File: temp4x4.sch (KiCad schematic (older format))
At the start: 17 parts

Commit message: updated schematic
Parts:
- removed J? (x3): 4-wire RTD, symbol Connector:Screw_Terminal_01x04
- added C? (x9): C, symbol Device:C
- added J?: 4-wire RTD, symbol Connector:Screw_Terminal_01x04
- added R? (x7): R, symbol Device:R
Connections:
- net Earth: now also C?.1, C?.1, C?.1, C?.2, C?.2, C?.2
- net ENABLE: now reaches U?.3 (EN)
- net ENABLE: now also J?.6 (Pin_6)
- net at U?.29 (REFN0): now also C?.2, C?.2, R?.2
- net at U?.3 (AIN4): now also C?.2, C?.2, R?.2
- net at U?.30 (REFP0): now also C?.1, C?.1, R?.2
- net at U?.4 (AIN3): now also C?.1, C?.1, R?.2
- net at U?.5 (AIN2): now also C?.2, C?.2, R?.2
- net at U?.6 (AIN1): now also C?.1, C?.1, R?.2
- net at U?.7 (AIN0): now also J?.1 (Pin_1)
- net at J?.2 (Pin_2): now also R?.1
- net at J?.3 (Pin_3): now also R?.1
- net at J?.4 (Pin_4): now also J?.1 (Pin_1)
- new net: J?.2 (Pin_2), R?.1
- new net: J?.3 (Pin_3), R?.1
- new net: J?.4 (Pin_4), R?.1, R?.1
- new net: R?.1, R?.2
- no-connect marks 5 -> 4
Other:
- moved on the sheet: C?, J?

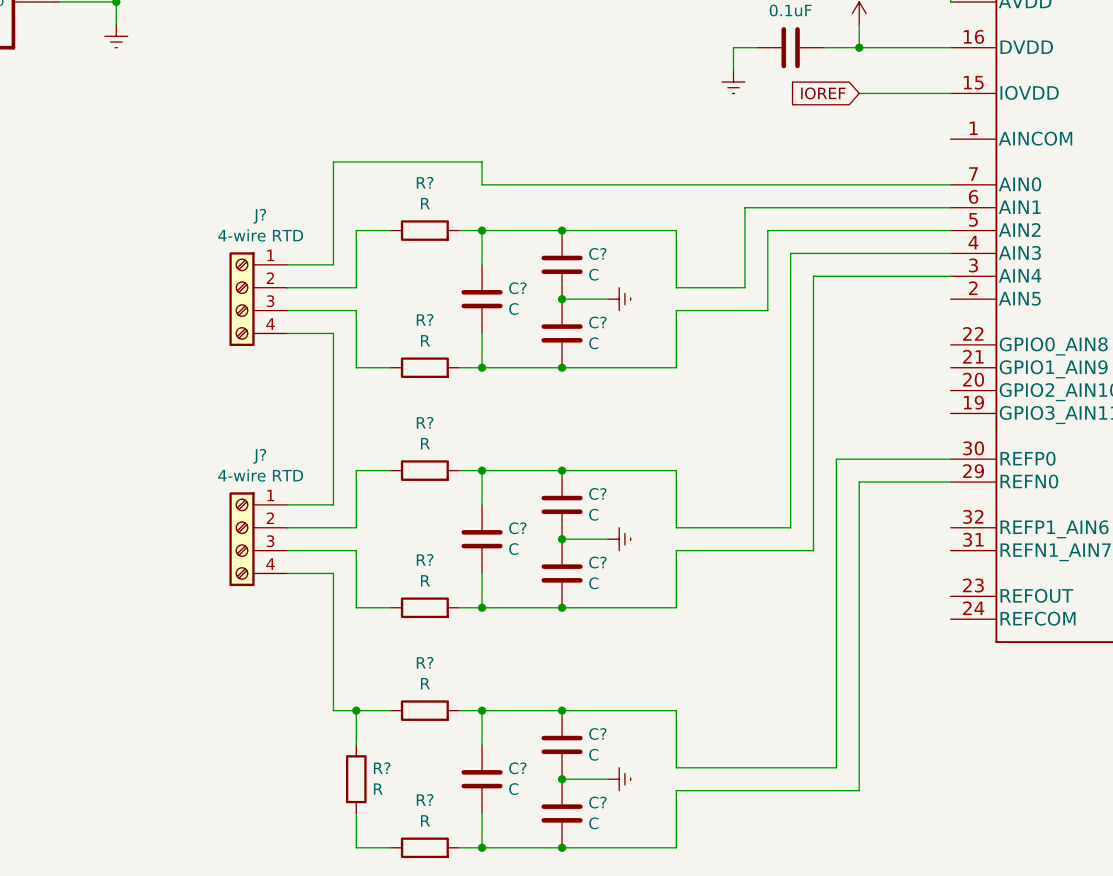
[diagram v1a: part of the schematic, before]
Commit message: added hierarchical sheet for RTDs
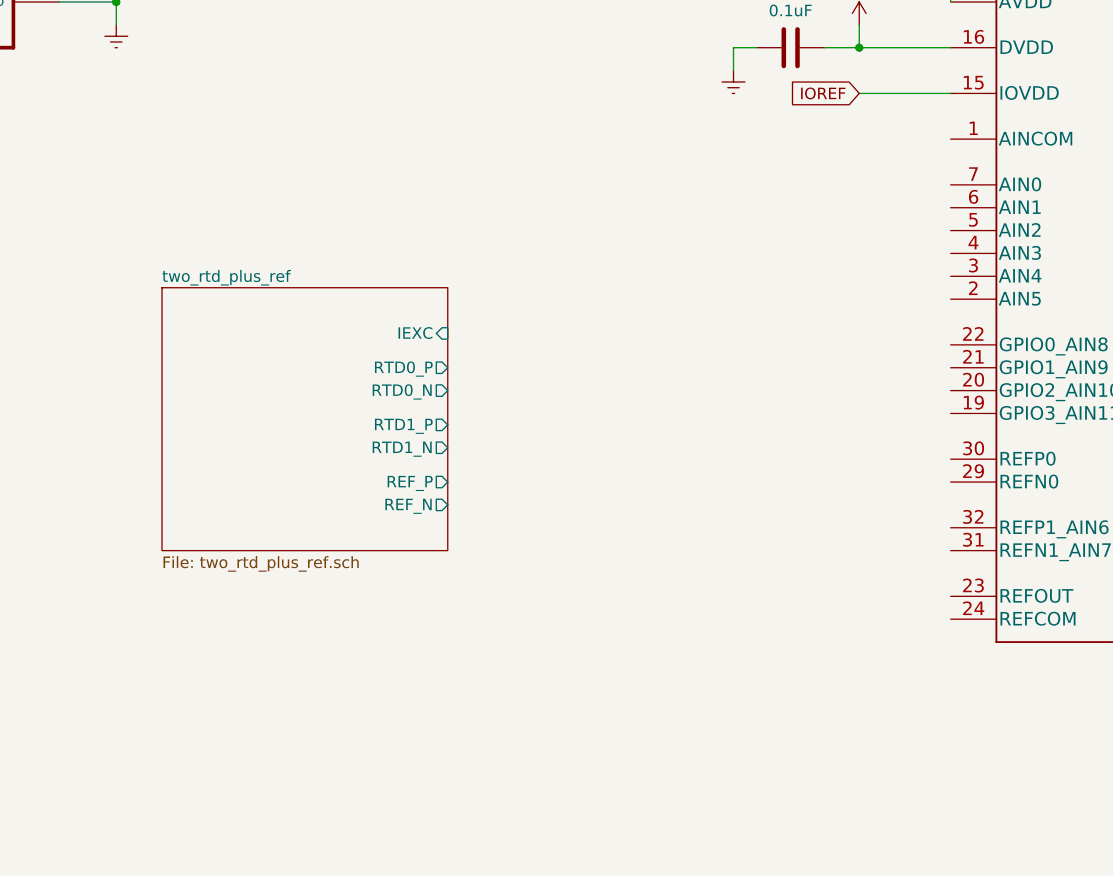
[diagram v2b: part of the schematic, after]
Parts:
- removed C? (x9): C, symbol Device:C
- removed J? (x2): 4-wire RTD, symbol Connector:Screw_Terminal_01x04
- removed R? (x7): R, symbol Device:R

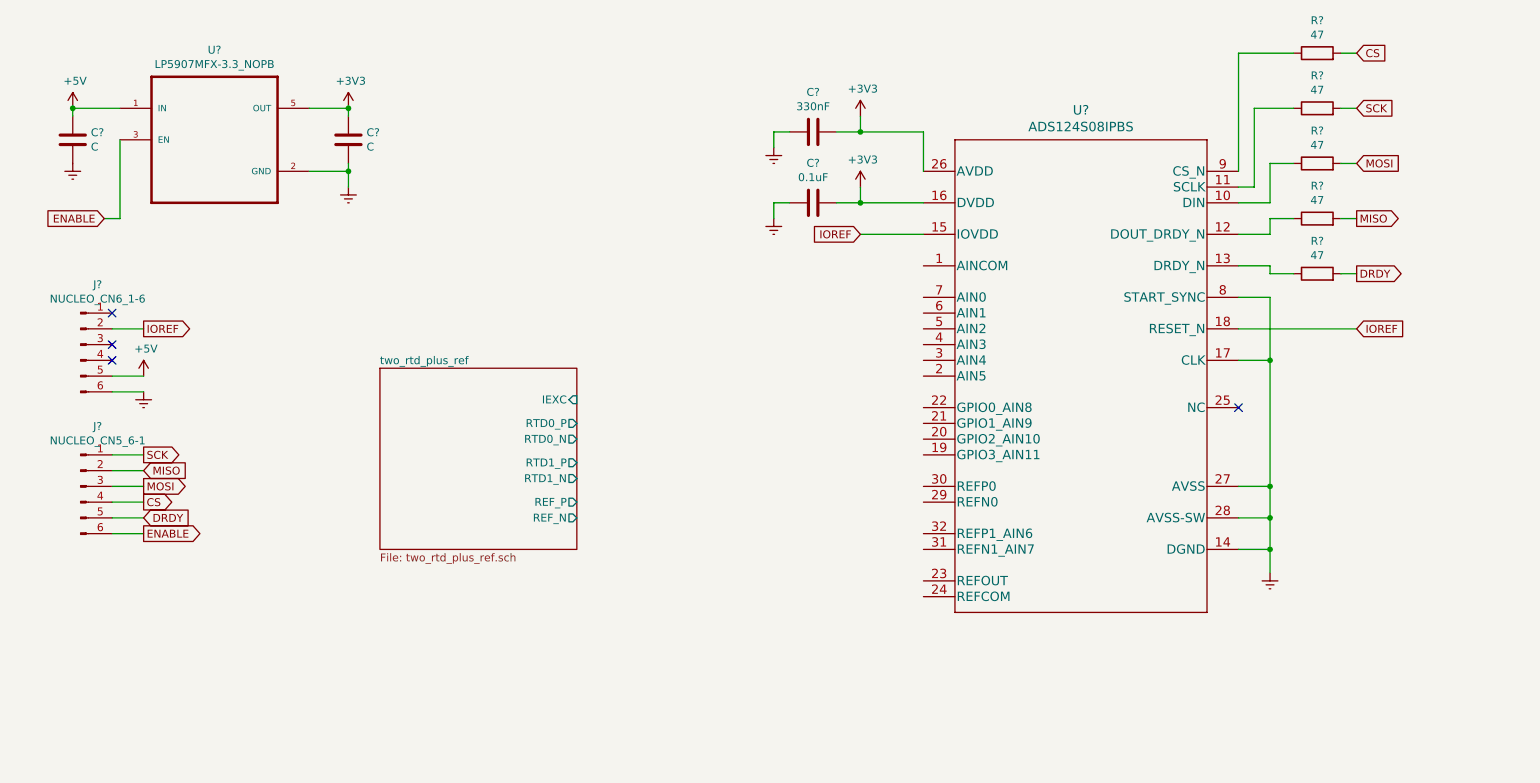
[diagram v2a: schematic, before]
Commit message: Added second set of RTDs
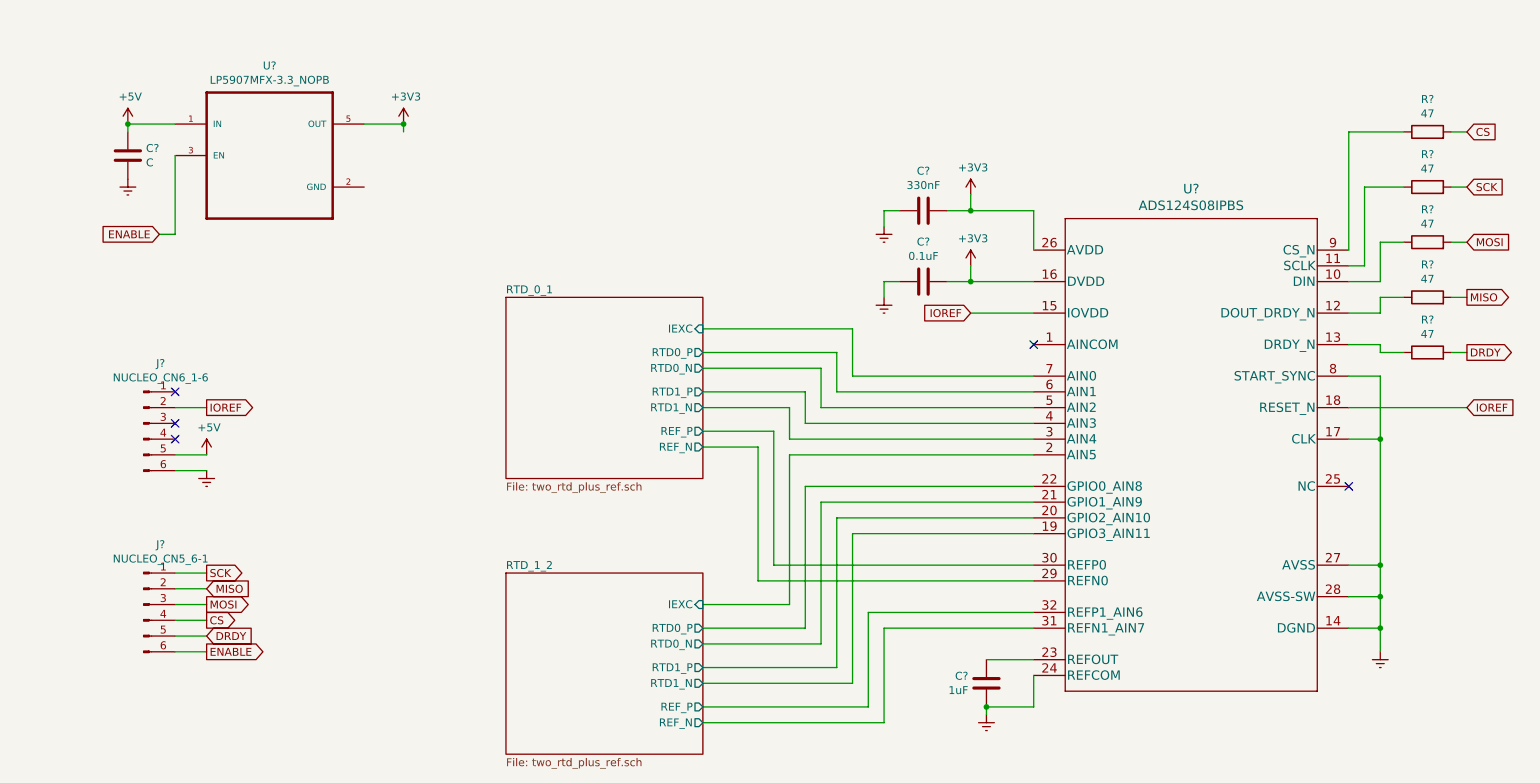
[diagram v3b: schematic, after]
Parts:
- C?: value C -> 1uF
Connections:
- net +3V3: no longer C?.1
- net Earth: now also U?.24 (REFCOM); no longer U?.2 (GND)
- net RTD_1_2/RTD1_N: now reaches U?.19 (GPIO3_AIN11)
- net RTD_1_2/IEXC: now reaches U?.2 (AIN5)
- net RTD_1_2/RTD1_P: now reaches U?.20 (GPIO2_AIN10)
- net RTD_1_2/RTD0_N: now reaches U?.21 (GPIO1_AIN9)
- net RTD_1_2/RTD0_P: now reaches U?.22 (GPIO0_AIN8)
- net at U?.23 (REFOUT): now also C?.1
- net RTD_0_1/REF_N: now reaches U?.29 (REFN0)
- net RTD_0_1/RTD1_N: now reaches U?.3 (AIN4)
- net RTD_0_1/REF_P: now reaches U?.30 (REFP0)
- net RTD_1_2/REF_N: now reaches U?.31 (REFN1_AIN7)
- net RTD_1_2/REF_P: now reaches U?.32 (REFP1_AIN6)
- net RTD_0_1/RTD1_P: now reaches U?.4 (AIN3)
- net RTD_0_1/RTD0_N: now reaches U?.5 (AIN2)
- net RTD_0_1/RTD0_P: now reaches U?.6 (AIN1)
- net RTD_0_1/IEXC: now reaches U?.7 (AIN0)
- no-connect marks 4 -> 5
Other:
- moved on the sheet: C?, J?, R?, U?

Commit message: completed schematic
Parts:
- added C2: 1uF, symbol Device:C
- added C5: 0.1uF, symbol Device:C
- C1: renamed from C?; value C -> 1uF
- gave numbers to parts that had none: 12
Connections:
- net +3V3: now also C2.1
- net Earth: now also U1.2 (GND), C2.2, C5.1
- net IOREF: now also C5.2
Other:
- moved on the sheet: C3, C4

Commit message: finished schematic, assigned footprints, generated netlist
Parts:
- C1, C2, C3, C4, C5, C6: footprint (none) -> Capacitor_SMD:C_0805_2012Metric_Pad1.15x1.40mm_HandSolder
- J1, J2: footprint (none) -> Connector_PinHeader_2.54mm:PinHeader_1x06_P2.54mm_Vertical
- R1, R2, R3, R4, R5: footprint (none) -> Resistor_SMD:R_0805_2012Metric_Pad1.15x1.40mm_HandSolder
- U1: footprint SOT95P280X145-5N -> Package_TO_SOT_SMD:SOT-23-5_HandSoldering
- U2: footprint PBS0032A_N -> Package_QFP:LQFP-32_5x5mm_P0.5mm
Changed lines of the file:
@@
 F 0 "U1" H 2150 2020 50  0000 C CNN
 F 1 "LP5907MFX-3.3_NOPB" H 2150 1929 50  0000 C CNN
-F 2 "SOT95P280X145-5N" H 2150 1450 50  0001 L BNN
+F 2 "Package_TO_SOT_SMD:SOT-23-5_HandSoldering" H 2150 1450 50  0001 L BNN
 F 3 "LP5907MFX-3.3/NOPB" H 2150 1450 50  0001 L BNN
 F 4 "SOT-23 Texas Instruments" H 2150 1450 50  0001 L BNN "Field4"
@@
 F 0 "C1" H 1365 1496 50  0000 L CNN
 F 1 "1uF" H 1365 1405 50  0000 L CNN
-F 2 "" H 1288 1300 50  0001 C CNN
+F 2 "Capacitor_SMD:C_0805_2012Metric_Pad1.15x1.40mm_HandSolder" H 1288 1300 50  0001 C CNN
 F 3 "~" H 1250 1450 50  0001 C CNN
 	1    1250 1450
@@
 F 0 "C6" H 6815 4846 50  0000 L CNN
 F 1 "1uF" H 6815 4755 50  0000 L CNN
-F 2 "" H 6738 4650 50  0001 C CNN
+F 2 "Capacitor_SMD:C_0805_2012Metric_Pad1.15x1.40mm_HandSolder" H 6738 4650 50  0001 C CNN
 F 3 "~" H 6700 4800 50  0001 C CNN
 	1    6700 4800
@@
 F 0 "R1" V 9707 1300 50  0000 C CNN
 F 1 "47" V 9616 1300 50  0000 C CNN
-F 2 "" V 9430 1300 50  0001 C CNN
+F 2 "Resistor_SMD:R_0805_2012Metric_Pad1.15x1.40mm_HandSolder" V 9430 1300 50  0001 C CNN
 F 3 "~" H 9500 1300 50  0001 C CNN
 	1    9500 1300
@@
 F 0 "R2" V 9707 1650 50  0000 C CNN
 F 1 "47" V 9616 1650 50  0000 C CNN
-F 2 "" V 9430 1650 50  0001 C CNN
+F 2 "Resistor_SMD:R_0805_2012Metric_Pad1.15x1.40mm_HandSolder" V 9430 1650 50  0001 C CNN
 F 3 "~" H 9500 1650 50  0001 C CNN
 	1    9500 1650
@@
 F 0 "R3" V 9707 2000 50  0000 C CNN
 F 1 "47" V 9616 2000 50  0000 C CNN
-F 2 "" V 9430 2000 50  0001 C CNN
+F 2 "Resistor_SMD:R_0805_2012Metric_Pad1.15x1.40mm_HandSolder" V 9430 2000 50  0001 C CNN
 F 3 "~" H 9500 2000 50  0001 C CNN
 	1    9500 2000
@@
 F 0 "R4" V 9707 2350 50  0000 C CNN
 F 1 "47" V 9616 2350 50  0000 C CNN
-F 2 "" V 9430 2350 50  0001 C CNN
+F 2 "Resistor_SMD:R_0805_2012Metric_Pad1.15x1.40mm_HandSolder" V 9430 2350 50  0001 C CNN
 F 3 "~" H 9500 2350 50  0001 C CNN
 	1    9500 2350
@@
 F 0 "R5" V 9707 2700 50  0000 C CNN
 F 1 "47" V 9616 2700 50  0000 C CNN
-F 2 "" V 9430 2700 50  0001 C CNN
+F 2 "Resistor_SMD:R_0805_2012Metric_Pad1.15x1.40mm_HandSolder" V 9430 2700 50  0001 C CNN
 F 3 "~" H 9500 2700 50  0001 C CNN
 	1    9500 2700
@@
 F 0 "J1" H 1322 3124 50  0000 R CNN
 F 1 "NUCLEO_CN6_1-6" H 1322 3033 50  0000 R CNN
-F 2 "" H 1350 3150 50  0001 C CNN
+F 2 "Connector_PinHeader_2.54mm:PinHeader_1x06_P2.54mm_Vertical" H 1350 3150 50  0001 C CNN
 F 3 "~" H 1350 3150 50  0001 C CNN
 	1    1350 3150
@@
 F 0 "J2" H 1322 4274 50  0000 R CNN
 F 1 "NUCLEO_CN5_6-1" H 1322 4183 50  0000 R CNN
-F 2 "" H 1350 4300 50  0001 C CNN
+F 2 "Connector_PinHeader_2.54mm:PinHeader_1x06_P2.54mm_Vertical" H 1350 4300 50  0001 C CNN
 F 3 "~" H 1350 4300 50  0001 C CNN
 	1    1350 4300
@@
 F 0 "C4" V 6102 1550 50  0000 C CNN
 F 1 "0.1uF" V 6011 1550 50  0000 C CNN
-F 2 "" H 5888 1400 50  0001 C CNN
+F 2 "Capacitor_SMD:C_0805_2012Metric_Pad1.15x1.40mm_HandSolder" H 5888 1400 50  0001 C CNN
 F 3 "~" H 5850 1550 50  0001 C CNN
 	1    5850 1550
@@
 F 0 "C3" V 6102 1100 50  0000 C CNN
 F 1 "330nF" V 6011 1100 50  0000 C CNN
-F 2 "" H 5888 950 50  0001 C CNN
+F 2 "Capacitor_SMD:C_0805_2012Metric_Pad1.15x1.40mm_HandSolder" H 5888 950 50  0001 C CNN
 F 3 "~" H 5850 1100 50  0001 C CNN
 	1    5850 1100
@@
 F 0 "U2" H 8000 5038 60  0000 C CNN
 F 1 "ADS124S08IPBS" H 8000 4932 60  0000 C CNN
-F 2 "PBS0032A_N" H 8000 3290 60  0001 C CNN
+F 2 "Package_QFP:LQFP-32_5x5mm_P0.5mm" H 8000 3290 60  0001 C CNN
 F 3 "" H 8000 3350 60  0000 C CNN
 	1    8000 3350
@@
 F 0 "C2" H 3115 1496 50  0000 L CNN
 F 1 "1uF" H 3115 1405 50  0000 L CNN
-F 2 "" H 3038 1300 50  0001 C CNN
+F 2 "Capacitor_SMD:C_0805_2012Metric_Pad1.15x1.40mm_HandSolder" H 3038 1300 50  0001 C CNN
 F 3 "~" H 3000 1450 50  0001 C CNN
 	1    3000 1450
@@
 F 0 "C5" V 6102 2000 50  0000 C CNN
 F 1 "0.1uF" V 6011 2000 50  0000 C CNN
-F 2 "" H 5888 1850 50  0001 C CNN
+F 2 "Capacitor_SMD:C_0805_2012Metric_Pad1.15x1.40mm_HandSolder" H 5888 1850 50  0001 C CNN
 F 3 "~" H 5850 2000 50  0001 C CNN
 	1    5850 2000

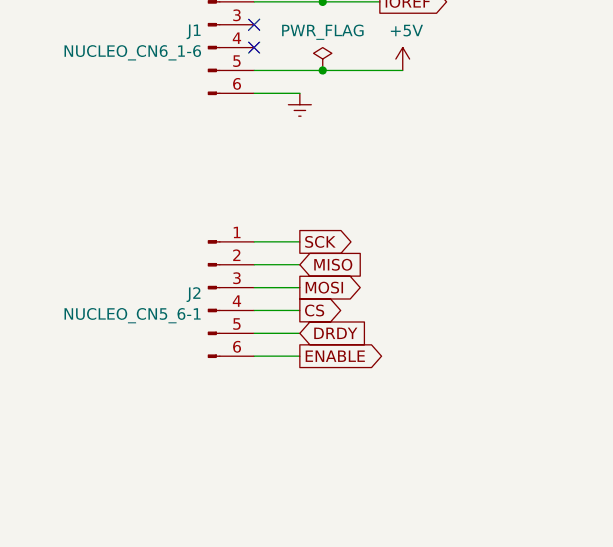
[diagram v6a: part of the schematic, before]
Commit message: made board bigger to allow for better separation of analog / digital domains
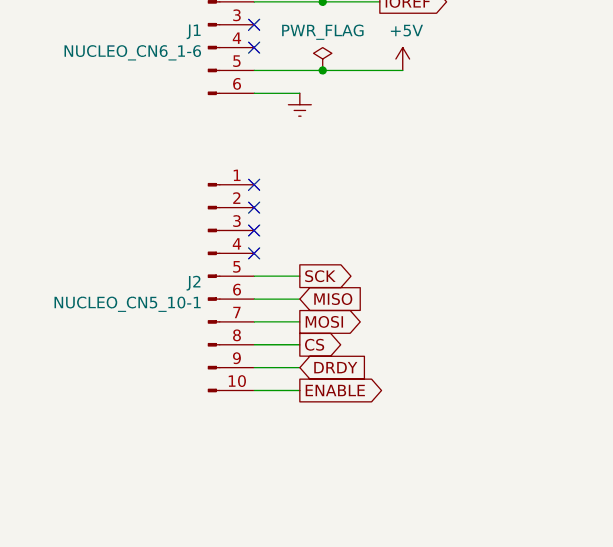
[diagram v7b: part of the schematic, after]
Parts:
- removed J2: NUCLEO_CN5_6-1, Connector_PinHeader_2.54mm:PinHeader_1x06_P2.54mm_Vertical, symbol Connector:Conn_01x06_Male
- added J2: NUCLEO_CN5_10-1, Connector_PinHeader_2.54mm:PinHeader_1x10_P2.54mm_Vertical, symbol Connector:Conn_01x10_Male
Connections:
- net CS: now also J2.8 (Pin_8)
- net DRDY: now also J2.9 (Pin_9)
- net ENABLE: now also J2.10 (Pin_10)
- net MISO: now also J2.6 (Pin_6)
- net MOSI: now also J2.7 (Pin_7)
- net SCK: now also J2.5 (Pin_5)
- no-connect marks 5 -> 9
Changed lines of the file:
@@
 Text GLabel 2100 3050 2    50   Output ~ 0
 IOREF
-Text GLabel 1750 4100 2    50   Output ~ 0
+Text GLabel 1750 4250 2    50   Output ~ 0
 SCK
 $Comp
@@
 	1550 3450 1750 3450
 Wire Wire Line
-	1550 4100 1750 4100
-Wire Wire Line
-	1550 4500 1750 4500
-Wire Wire Line
-	1550 4400 1750 4400
-Wire Wire Line
-	1550 4300 1750 4300
-Wire Wire Line
-	1550 4200 1750 4200
-Text GLabel 1750 4500 2    50   Input ~ 0
+	1550 4250 1750 4250
+Wire Wire Line
+	1550 4650 1750 4650
+Wire Wire Line
+	1550 4550 1750 4550
+Wire Wire Line
+	1550 4450 1750 4450
+Wire Wire Line
+	1550 4350 1750 4350
+Text GLabel 1750 4650 2    50   Input ~ 0
 DRDY
-Text GLabel 1750 4400 2    50   Output ~ 0
+Text GLabel 1750 4550 2    50   Output ~ 0
 CS
-Text GLabel 1750 4300 2    50   Output ~ 0
+Text GLabel 1750 4450 2    50   Output ~ 0
 MOSI
-Text GLabel 1750 4200 2    50   Input ~ 0
+Text GLabel 1750 4350 2    50   Input ~ 0
 MISO
-$Comp
-L Connector:Conn_01x06_Male J2
-U 1 1 5ECC8F38
-P 1350 4300
-F 0 "J2" H 1322 4274 50  0000 R CNN
-F 1 "NUCLEO_CN5_6-1" H 1322 4183 50  0000 R CNN
-F 2 "Connector_PinHeader_2.54mm:PinHeader_1x06_P2.54mm_Vertical" H 1350 4300 50  0001 C CNN
-F 3 "~" H 1350 4300 50  0001 C CNN
-	1    1350 4300
-	1    0    0    -1
-$EndComp
 $Comp
 L Device:C C4
@@
 Wire Wire Line
 	9200 2700 9350 2700
-Text GLabel 1750 4600 2    50   Output ~ 0
+Text GLabel 1750 4750 2    50   Output ~ 0
 ENABLE
 Text GLabel 1300 2200 0    50   Input ~ 0
 ENABLE
 Wire Wire Line
-	1550 4600 1750 4600
+	1550 4750 1750 4750
 Wire Wire Line
 	6000 1550 6150 1550
@@
 Wire Wire Line
 	1850 3350 2200 3350
+$Comp
+L Connector:Conn_01x10_Male J2
+U 1 1 5EC563AD
+P 1350 4250
+F 0 "J2" H 1322 4224 50  0000 R CNN
+F 1 "NUCLEO_CN5_10-1" H 1322 4133 50  0000 R CNN
+F 2 "Connector_PinHeader_2.54mm:PinHeader_1x10_P2.54mm_Vertical" H 1350 4250 50  0001 C CNN
+F 3 "~" H 1350 4250 50  0001 C CNN
+	1    1350 4250
+	1    0    0    -1
+$EndComp
+NoConn ~ 1550 4150
+NoConn ~ 1550 4050
+NoConn ~ 1550 3950
+NoConn ~ 1550 3850
 $EndSCHEMATC
